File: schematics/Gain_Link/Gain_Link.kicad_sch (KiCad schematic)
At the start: 13 parts, among them IC1 AD8221TRMZ-EP, IC3 AD8221TRMZ-EP, J1 PCIE-036-02-X-D-TH, J2 Conn_02x02_Odd_Even, J3 Conn_02x02_Odd_Even

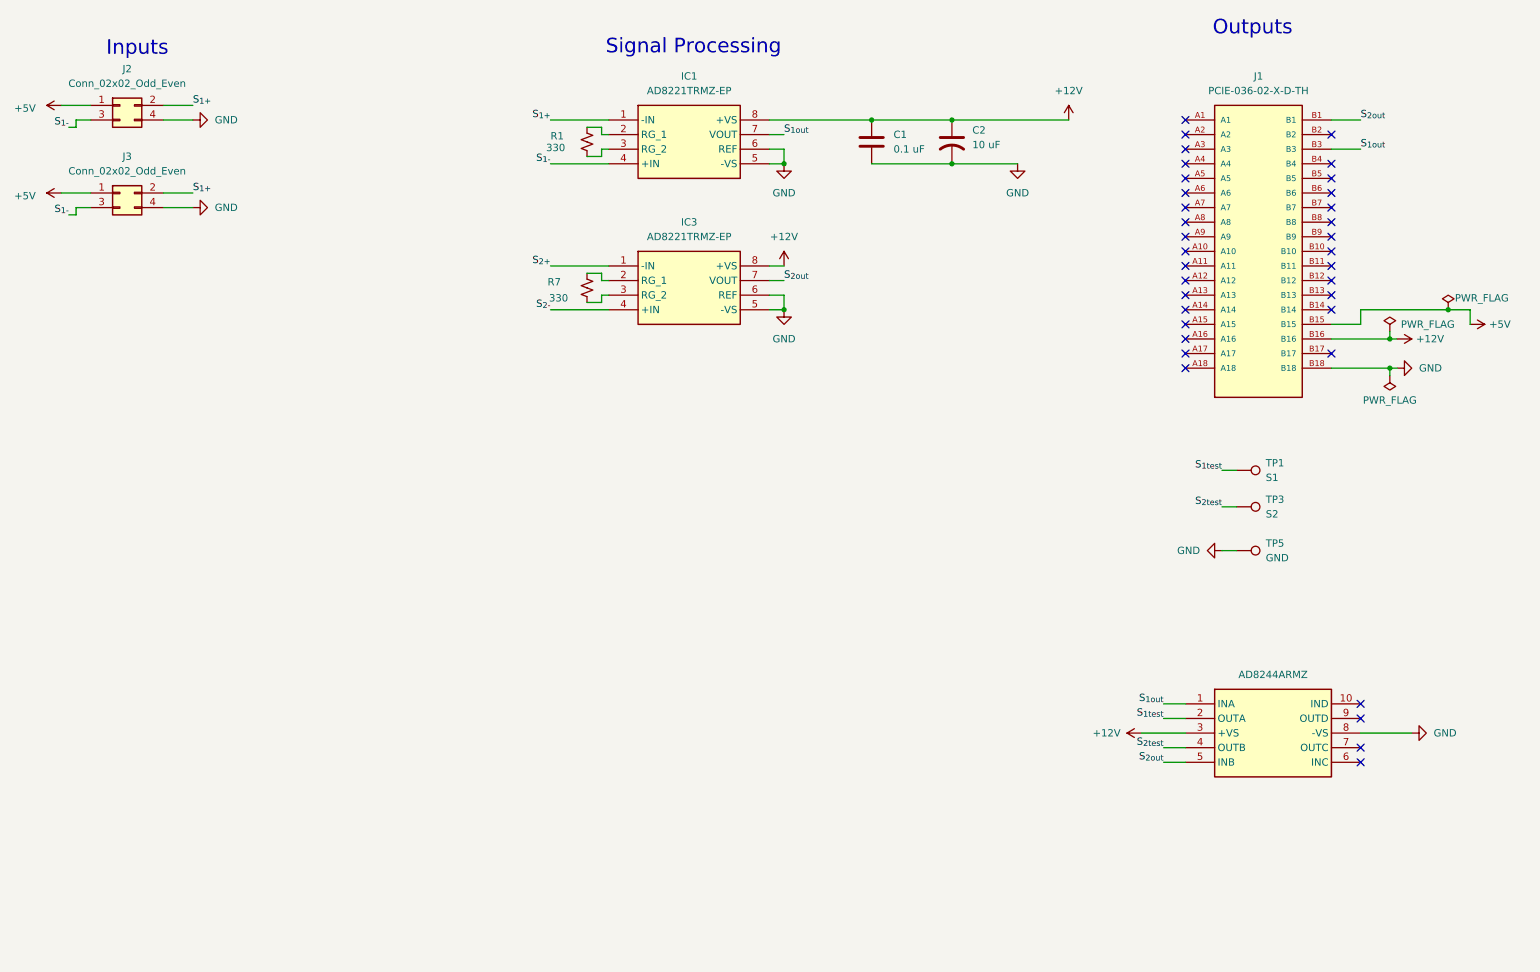
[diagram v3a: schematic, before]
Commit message: Measured out Board Components Added TVS Diodes Edited to be 4 layers (currently) 	-Top: Signals 	-Mid1: GND 	-Mid2: ?? 	-Bottom: +12V
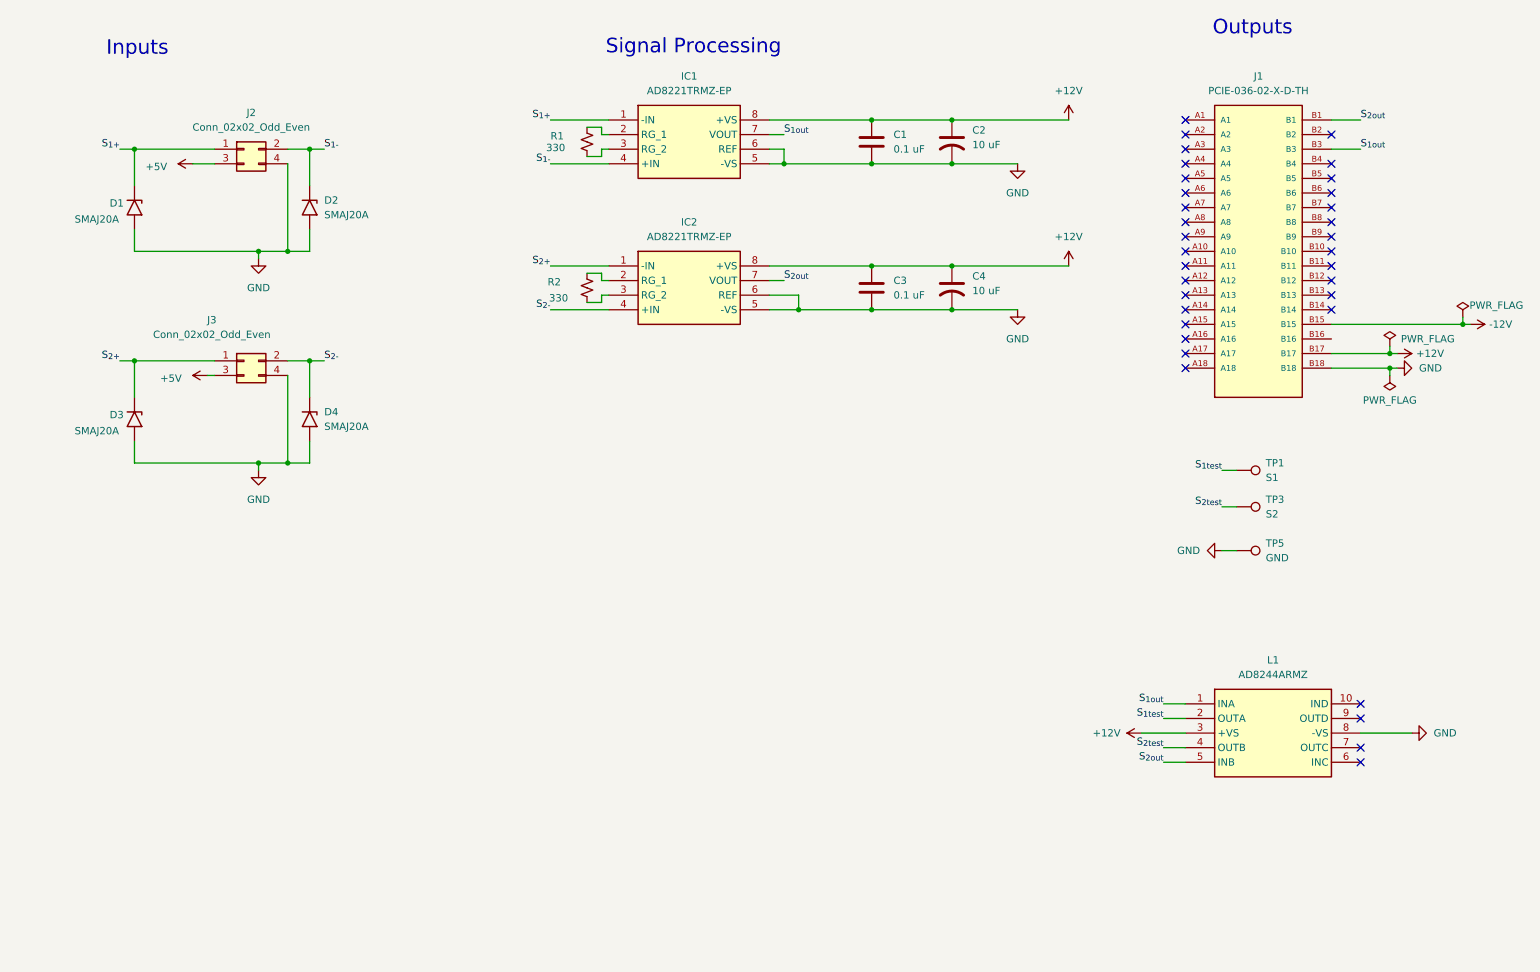
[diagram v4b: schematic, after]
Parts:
- added C3: 0.1 uF, Capacitor_SMD:C_0603_1608Metric, symbol Device:C
- added C4: 10 uF, Capacitor_SMD:C_0603_1608Metric, symbol Device:C_US
- added D1, D2, D3, D4: SMAJ20A, Diode_SMD:D_SMA, symbol Diode:SMAJ20A
- C1, C2: footprint Capacitor_SMD:C_1210_3225Metric -> Capacitor_SMD:C_0603_1608Metric
- IC1: footprint Link_Footprints:AD8221TRMZ-EP -> Link Footprints:AD8221TRMZ; symbol Link_Components:AD8221TRMZ-EP -> Link Components:AD8221TRMZ
- IC2: renamed from IC3; footprint Link_Footprints:AD8221TRMZ-EP -> Link Footprints:AD8221TRMZ; symbol Link_Components:AD8221TRMZ-EP -> Link Components:AD8221TRMZ
- J2, J3: footprint (none) -> Link Footprints:PC-1053864
- L1: footprint Link_Footprints:AD8244ARMZ -> Link Footprints:AD8244ARMZ; symbol Link_Components:AD8244ARMZ -> Link Components:AD8244ARMZ
- R1: footprint Resistor_SMD:R_2512_6332Metric -> Resistor_SMD:R_0805_2012Metric
- R2: renamed from R7; footprint Resistor_SMD:R_2512_6332Metric -> Resistor_SMD:R_0805_2012Metric
- TP1, TP3, TP5: footprint Link_Footprints:KEYSTONE_5017 -> Link Footprints:Keystone_5017
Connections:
- net +12V: now also J1.B17, C3.1, C4.1; no longer J1.B16
- net +5V: now also J2.3 (Pin_3), J3.3 (Pin_3); no longer J1.B15, J2.1 (Pin_1), J3.1 (Pin_1)
- net GND: now also C3.2, C4.2, D1.2 (A2), D2.2 (A2), D3.2 (A2), D4.2 (A2)
- net S_{1+}: now also J2.1 (Pin_1), D1.1 (A1); no longer J2.2 (Pin_2), J3.2 (Pin_2)
- net S_{1-}: now also J2.2 (Pin_2), D2.1 (A1); no longer J2.3 (Pin_3), J3.3 (Pin_3)
- net S_{2+}: now also J3.1 (Pin_1), D3.1 (A1)
- net S_{2-}: now also J3.2 (Pin_2), D4.1 (A1)
- new net -12V: J1.B15
- no-connect marks 35 -> 34
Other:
- moved on the sheet: J2, J3

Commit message: Replaced AD8221 with INA849, made board smaller
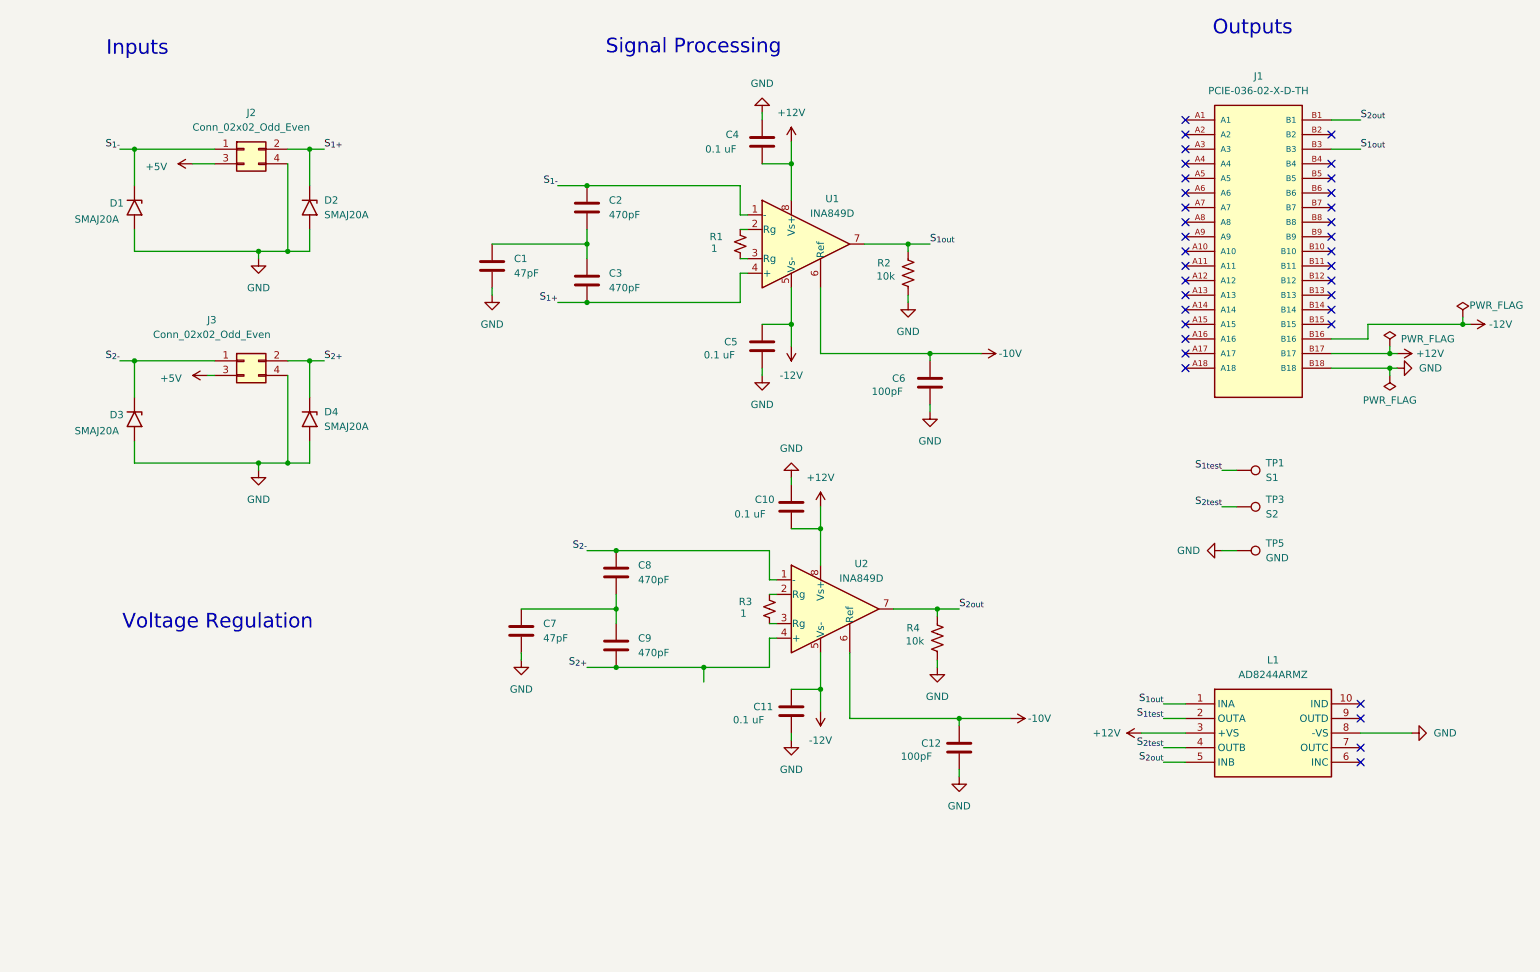
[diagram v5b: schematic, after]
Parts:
- removed C2, C4: 10 uF, Capacitor_SMD:C_0603_1608Metric, symbol Device:C_US
- removed IC1, IC2: AD8221TRMZ-EP, Link Footprints:AD8221TRMZ, symbol Link Components:AD8221TRMZ
- removed R2: 330, Resistor_SMD:R_0805_2012Metric, symbol Device:R_Small_US
- added C1, C7: 47pF, Capacitor_SMD:C_0603_1608Metric, symbol Device:C
- added C10, C11, C5: 0.1 uF, Capacitor_SMD:C_0603_1608Metric, symbol Device:C
- added C12, C6: 100pF, Capacitor_SMD:C_0603_1608Metric, symbol Device:C
- added C2, C8, C9: 470pF, Capacitor_SMD:C_0603_1608Metric, symbol Device:C
- added R2, R4: 10k, Resistor_SMD:R_0805_2012Metric, symbol Device:R_US
- added R3: 1, Resistor_SMD:R_0805_2012Metric, symbol Device:R_Small_US
- added U1, U2: INA849D, Link Footprints:INA849, symbol Link Components:INA849D
- C3: value 0.1 uF -> 470pF
- R1: value 330 -> 1
- renumbered C1 to C4
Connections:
- net +12V: now also C10.1, U1.8 (Vs+), U2.8 (Vs+); no longer C3.1
- net -12V: now also J1.B16, C11.1, C5.1, U1.5 (Vs-), U2.5 (Vs-); no longer J1.B15
- net GND: now also C1.1, C10.2, C11.2, C12.2, C5.2, C6.2, C7.1, R2.1, R4.1; no longer C3.2
- net S_{1+}: now also C3.1, D2.1 (A1), J2.2 (Pin_2), U1.4 (+); no longer D1.1 (A1), J2.1 (Pin_1)
- net S_{1-}: now also D1.1 (A1), J2.1 (Pin_1), C2.2, U1.1 (-); no longer D2.1 (A1), J2.2 (Pin_2)
- net S_{1out}: now also R2.2, U1.7
- net S_{2+}: now also D4.1 (A1), J3.2 (Pin_2), C9.1, U2.4 (+); no longer D3.1 (A1), J3.1 (Pin_1)
- net S_{2-}: now also D3.1 (A1), J3.1 (Pin_1), C8.2, U2.1 (-); no longer D4.1 (A1), J3.2 (Pin_2)
- net S_{2out}: now also R4.2, U2.7
- net at R1.1: now also U1.2 (Rg)
- net at R1.2: now also U1.3 (Rg)
- new net: R3.1, U2.2 (Rg)
- new net: R3.2, U2.3 (Rg)
- new net: C1.2, C2.1, C3.2
- new net: C7.2, C8.1, C9.2
- new net -10V: C12.1, C6.1, U1.6 (Ref), U2.6 (Ref)
- no-connect marks 34 -> 35
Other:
- note added: "Voltage Regulation"
- moved on the sheet: C4, R1

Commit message: feat(gain-link): Started a signal chain sub sheet
Signed-off-by: Andrew Balmos <andrew@balmos.org>
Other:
- added sheet Sig_1 (signal.kicad_sch)
- added sheet Sig_2 (signal.kicad_sch)
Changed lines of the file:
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@@
+		)
+	)
+	(sheet
+		(at 97.79 165.1)
+		(size 12.7 12.7)
+		(exclude_from_sim no)
+		(in_bom yes)
+		(on_board yes)
+		(dnp no)
+		(fields_autoplaced yes)
+		(stroke
+			(width 0.1524)
+			(type solid)
+		)
+		(fill
+			(color 0 0 0 0.0000)
+		)
+		(property "Sheetname" "Sig_2"
+			(at 97.79 164.3884 0)
+			(effects
+				(font
+					(size 1.27 1.27)
+				)
+				(justify left bottom)
+			)
+		)
+		(property "Sheetfile" "signal.kicad_sch"
+			(at 97.79 178.3846 0)
+			(effects
+				(font
+					(size 1.27 1.27)
+				)
+				(justify left top)
+			)
+		)
+		(pin "Vin_m" input
+			(at 97.79 168.91 180)
+			(effects
+				(font
+					(size 1.27 1.27)
+				)
+				(justify left)
+			)
+		)
+		(pin "Vout" input
+			(at 110.49 171.45 0)
+			(effects
+				(font
+					(size 1.27 1.27)
+				)
+				(justify right)
+			)
+		)
+		(pin "Vin_p" input
+			(at 97.79 173.99 180)
+			(effects
+				(font
+					(size 1.27 1.27)
+				)
+				(justify left)
+			)
+		)
+		(instances
+			(project "Gain_Link"
+				(path "/044df771-0288-4dc4-a604-257e905d1378"
+					(page "3")
+				)
+			)
+		)
+	)
+	(sheet
+		(at 64.77 163.83)
+		(size 12.7 12.7)
+		(exclude_from_sim no)
+		(in_bom yes)
+		(on_board yes)
+		(dnp no)
+		(fields_autoplaced yes)
+		(stroke
+			(width 0.1524)
+			(type solid)
+		)
+		(fill
+			(color 0 0 0 0.0000)
+		)
+		(property "Sheetname" "Sig_1"
+			(at 64.77 163.1184 0)
+			(effects
+				(font
+					(size 1.27 1.27)
+				)
+				(justify left bottom)
+			)
+		)
+		(property "Sheetfile" "signal.kicad_sch"
+			(at 64.77 177.1146 0)
+			(effects
+				(font
+					(size 1.27 1.27)
+				)
+				(justify left top)
+			)
+		)
+		(pin "Vin_m" input
+			(at 64.77 167.64 180)
+			(effects
+				(font
+					(size 1.27 1.27)
+				)
+				(justify left)
+			)
+		)
+		(pin "Vout" input
+			(at 77.47 170.18 0)
+			(effects
+				(font
+					(size 1.27 1.27)
+				)
+				(justify right)
+			)
+		)
+		(pin "Vin_p" input
+			(at 64.77 172.72 180)
+			(effects
+				(font
+					(size 1.27 1.27)
+				)
+				(justify left)
+			)
+		)
+		(instances
+			(project "Gain_Link"
+				(path "/044df771-0288-4dc4-a604-257e905d1378"
+					(page "2")
+				)
+			)
 		)
 	)
